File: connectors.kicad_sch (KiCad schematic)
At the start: 4 parts, among them J1 Conn_01x04_Pin, J2 Conn_01x04_Pin, J3 Conn_01x09_Pin, J4 Conn_02x03_Odd_Even

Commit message: Assigned footprints to symbols
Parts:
- J1, J2: footprint (none) -> Connector_PinHeader_2.54mm:PinHeader_1x04_P2.54mm_Vertical
- J3: footprint (none) -> Connector_PinHeader_2.54mm:PinHeader_1x09_P2.54mm_Vertical
- J4: footprint (none) -> Connector_PinHeader_2.54mm:PinHeader_2x03_P2.54mm_Vertical
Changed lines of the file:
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@@
 			)
 		)
-		(property "Footprint" ""
+		(property "Footprint" "Connector_PinHeader_2.54mm:PinHeader_1x09_P2.54mm_Vertical"
 			(at 143.51 67.31 0)
 			(effects
@@
 			)
 		)
-		(property "Footprint" ""
+		(property "Footprint" "Connector_PinHeader_2.54mm:PinHeader_1x04_P2.54mm_Vertical"
 			(at 93.98 62.23 0)
 			(effects
@@
 			)
 		)
-		(property "Footprint" ""
+		(property "Footprint" "Connector_PinHeader_2.54mm:PinHeader_2x03_P2.54mm_Vertical"
 			(at 95.25 90.17 0)
 			(effects
@@
 			)
 		)
-		(property "Footprint" ""
+		(property "Footprint" "Connector_PinHeader_2.54mm:PinHeader_1x04_P2.54mm_Vertical"
 			(at 114.3 60.96 0)
 			(effects

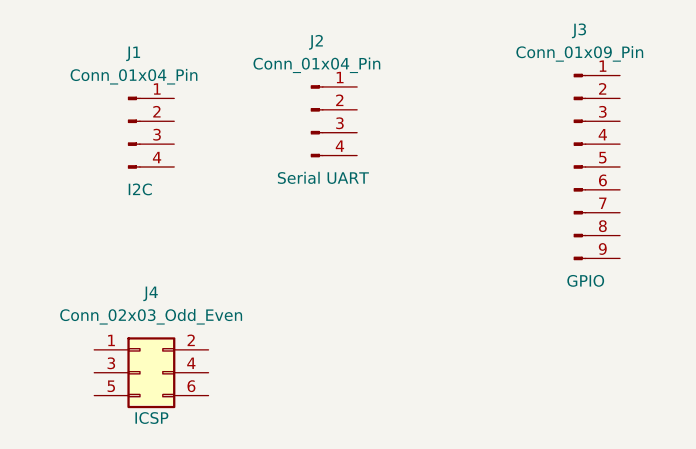
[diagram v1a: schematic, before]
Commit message: Completed wiring in secondary sheet
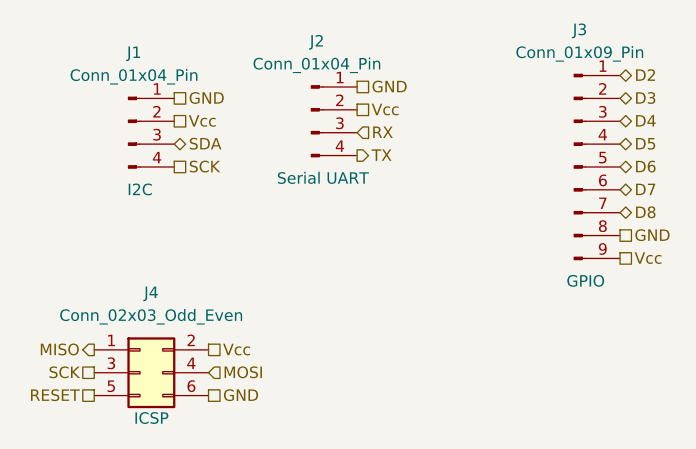
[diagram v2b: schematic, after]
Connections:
- net D2: now reaches J3.1 (Pin_1)
- net D3: now reaches J3.2 (Pin_2)
- net D4: now reaches J3.3 (Pin_3)
- net D5: now reaches J3.4 (Pin_4)
- net D6: now reaches J3.5 (Pin_5)
- net D7: now reaches J3.6 (Pin_6)
- net D8: now reaches J3.7 (Pin_7)
- net GND: now reaches J3.8 (Pin_8)
- net GND: now also J1.1 (Pin_1), J2.1 (Pin_1), J4.6 (Pin_6)
- net Vcc: now reaches J3.9 (Pin_9)
- net Vcc: now also J1.2 (Pin_2), J2.2 (Pin_2), J4.2 (Pin_2)
- net SDA: now reaches J1.3 (Pin_3)
- net SCK: now reaches J1.4 (Pin_4)
- net SCK: now also J4.3 (Pin_3)
- net MISO: now reaches J4.1 (Pin_1)
- net MOSI: now reaches J4.4 (Pin_4)
- net RESET: now reaches J4.5 (Pin_5)
- net RX: now reaches J2.3 (Pin_3)
- net TX: now reaches J2.4 (Pin_4)
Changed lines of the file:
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@@
 	(generator_version "9.0")
 	(paper "A4")
+	(hierarchical_label "D2"
+		(shape bidirectional)
+		(at 148.59 57.15 0)
+		(effects
+			(font
+				(size 1.27 1.27)
+			)
+			(justify left)
+		)
+	)
+	(hierarchical_label "MISO"
+		(shape output)
+		(at 90.17 87.63 180)
+		(effects
+			(font
+				(size 1.27 1.27)
+			)
+			(justify right)
+		)
+	)
+	(hierarchical_label "GND"
+		(shape passive)
+		(at 99.06 59.69 0)
+		(effects
+			(font
+				(size 1.27 1.27)
+			)
+			(justify left)
+		)
+	)
+	(hierarchical_label "GND"
+		(shape passive)
+		(at 148.59 74.93 0)
+		(effects
+			(font
+				(size 1.27 1.27)
+			)
+			(justify left)
+		)
+	)
+	(hierarchical_label "D5"
+		(shape bidirectional)
+		(at 148.59 64.77 0)
+		(effects
+			(font
+				(size 1.27 1.27)
+			)
+			(justify left)
+		)
+	)
+	(hierarchical_label "D6"
+		(shape bidirectional)
+		(at 148.59 67.31 0)
+		(effects
+			(font
+				(size 1.27 1.27)
+			)
+			(justify left)
+		)
+	)
+	(hierarchical_label "D4"
+		(shape bidirectional)
+		(at 148.59 62.23 0)
+		(effects
+			(font
+				(size 1.27 1.27)
+			)
+			(justify left)
+		)
+	)
+	(hierarchical_label "D7"
+		(shape bidirectional)
+		(at 148.59 69.85 0)
+		(effects
+			(font
+				(size 1.27 1.27)
+			)
+			(justify left)
+		)
+	)
+	(hierarchical_label "Vcc"
+		(shape passive)
+		(at 99.06 62.23 0)
+		(effects
+			(font
+				(size 1.27 1.27)
+			)
+			(justify left)
+		)
+	)
+	(hierarchical_label "Vcc"
+		(shape passive)
+		(at 148.59 77.47 0)
+		(effects
+			(font
+				(size 1.27 1.27)
+			)
+			(justify left)
+		)
+	)
+	(hierarchical_label "Vcc"
+		(shape passive)
+		(at 102.87 87.63 0)
+		(effects
+			(font
+				(size 1.27 1.27)
+			)
+			(justify left)
+		)
+	)
+	(hierarchical_label "SDA"
+		(shape bidirectional)
+		(at 99.06 64.77 0)
+		(effects
+			(font
+				(size 1.27 1.27)
+			)
+			(justify left)
+		)
+	)
+	(hierarchical_label "GND"
+		(shape passive)
+		(at 102.87 92.71 0)
+		(effects
+			(font
+				(size 1.27 1.27)
+			)
+			(justify left)
+		)
+	)
+	(hierarchical_label "D3"
+		(shape bidirectional)
+		(at 148.59 59.69 0)
+		(effects
+			(font
+				(size 1.27 1.27)
+			)
+			(justify left)
+		)
+	)
+	(hierarchical_label "GND"
+		(shape passive)
+		(at 119.38 58.42 0)
+		(effects
+			(font
+				(size 1.27 1.27)
+			)
+			(justify left)
+		)
+	)
+	(hierarchical_label "RX"
+		(shape input)
+		(at 119.38 63.5 0)
+		(effects
+			(font
+				(size 1.27 1.27)
+			)
+			(justify left)
+		)
+	)
+	(hierarchical_label "MOSI"
+		(shape input)
+		(at 102.87 90.17 0)
+		(effects
+			(font
+				(size 1.27 1.27)
+			)
+			(justify left)
+		)
+	)
+	(hierarchical_label "RESET"
+		(shape passive)
+		(at 90.17 92.71 180)
+		(effects
+			(font
+				(size 1.27 1.27)
+			)
+			(justify right)
+		)
+	)
+	(hierarchical_label "D8"
+		(shape bidirectional)
+		(at 148.59 72.39 0)
+		(effects
+			(font
+				(size 1.27 1.27)
+			)
+			(justify left)
+		)
+	)
+	(hierarchical_label "Vcc"
+		(shape passive)
+		(at 119.38 60.96 0)
+		(effects
+			(font
+				(size 1.27 1.27)
+			)
+			(justify left)
+		)
+	)
+	(hierarchical_label "TX"
+		(shape output)
+		(at 119.38 66.04 0)
+		(effects
+			(font
+				(size 1.27 1.27)
+			)
+			(justify left)
+		)
+	)
+	(hierarchical_label "SCK"
+		(shape passive)
+		(at 99.06 67.31 0)
+		(effects
+			(font
+				(size 1.27 1.27)
+			)
+			(justify left)
+		)
+	)
+	(hierarchical_label "SCK"
+		(shape passive)
+		(at 90.17 90.17 180)
+		(effects
+			(font
+				(size 1.27 1.27)
+			)
+			(justify right)
+		)
+	)
 	(symbol
 		(lib_id "Connector:Conn_01x09_Pin")
